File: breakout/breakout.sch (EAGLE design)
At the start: 241 parts, among them J17 1789074, J26 69168-124HLF, J29 SJ1-3514-SMT-TR, J31 69168-116HLF, J32 12226-8250-00FR, J33 1888276, J34 69168-116HLF, J35 1888276, Q1 SI1012R, Q2 SI1012R, Q3 SI1012R, Q4 SI1012R, Q5 SI1012R, Q6 SI1012R, Q7 SI1012R, Q8 SI1012R, Q9 IRFML8244TRPBF, U1 SK6805-E-J, U10 TXB0101, U11 SK6805-E-J, U12 SK6805-E-J, U13 SK6805-E-J, U14 SK6805-E-J, U15 SK6805-E-J, U16 SK6805-E-J, U17 SK6805-E-J, U18 SK6805-E-J, U19 SK6805-E-J, U2 SK6805-E-J, U20 SK6805-E-J, U21 SK6805-E-J, U22 SK6805-E-J, U23 SK6805-E-J, U24 SK6805-E-J, U25 SK6805-E-J, U26 SK6805-E-J, U27 SK6805-E-J, U28 SK6805-E-J, U29 SK6805-E-J, U3 SK6805-E-J, U30 SK6805-E-J, U31 SK6805-E-J, U32 SK6805-E-J, U33 SK6805-E-J, U34 SK6805-E-J, U35 SK6805-E-J, U36 SK6805-E-J, U37 SK6805-E-J, U38 SK6805-E-J, U39 SK6805-E-J, U4 SK6805-E-J, U40 SK6805-E-J, U41 SK6805-E-J, U42 SK6805-E-J, U43 G6K-2F-RF, U44 G6K-2F-RF, U45 G6K-2F-RF, U46 G6K-2F-RF, U47 LTM4622A, U48 SI8610, U49 TINY-FPGA-BX, U5 SK6805-E-J, U50 TCA9555, U51 FIN1032MTCX, U52 SN65LVDS9638DGN, U53 SN65LVDS9638DGN, U6 SK6805-E-J, U7 SK6805-E-J, U8 SK6805-E-J, U9 SK6805-E-J

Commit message: Updated the schematic to use Harp timestamp bus as input.
The layout (.brd) is not ready yet.

Replaced U48 SI8610 with U48 TLV70033DDCR (adds  extra BOM line. PN TLV70033DDCR)
Replaced C41 0402 0.1uF with C41 0805 10uF (same PN as C40 to not add extra BOM line)
Replaced C43 0402 0.1uF with C43 0805 10uF (same PN as C40 to not add extra BOM line)
Added R44 0402 13.3k (same PN as R19 to not add extra BOM line)
Added R45 0402 10R (adds extra BOM line. PN CRCW040210R0FKEDHP)

New BOM lines: 2
Replaced components: 3
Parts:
- added R44: 13.3k, jonnew:R_0402
- added R45: 10R, jonnew:R_0402
- C41, C43: value 0.1uF -> 10uF; device jonnew:C_0402 -> jonnew:C_0805
- U48: value SI8610 -> TLV70033DDCR; device CNP-ics 2:SI8610 -> harp input expander:TLV700XX; MPN (none) -> TLV70033DDCR; NOTES (none) -> -; TYPE (none) -> SMD
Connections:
- removed net HARP_CLKOUT: U48.A1, U49.24
- removed net N$17: C41.2, J29.5, U48.BGND
- removed net N$18: J29.4, U48.B1
- new net HARP_CLKIN: J29.4, R44.2, U49.24
- new net N$85: C43.1, R45.1, U48.OUT
- net +5V0: now also C41.1, U48.EN, U48.IN; no longer C43.2, U48.AVDD
- net GND: now also C41.2, C43.2, J29.5, U48.GND; no longer C43.1, U48.AGND
- net N$16: now also R44.1, R45.2; no longer C41.1, U48.BVDD
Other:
- note added: "HARP_CLKIN signal has the serial comunication/protocol that is synchronizing all the Harp devices."
- note removed: "CLKOUT signal has the serial comunication/protocol that will sync all the Harp devices."
- moved on the sheet: C41, C43, J29

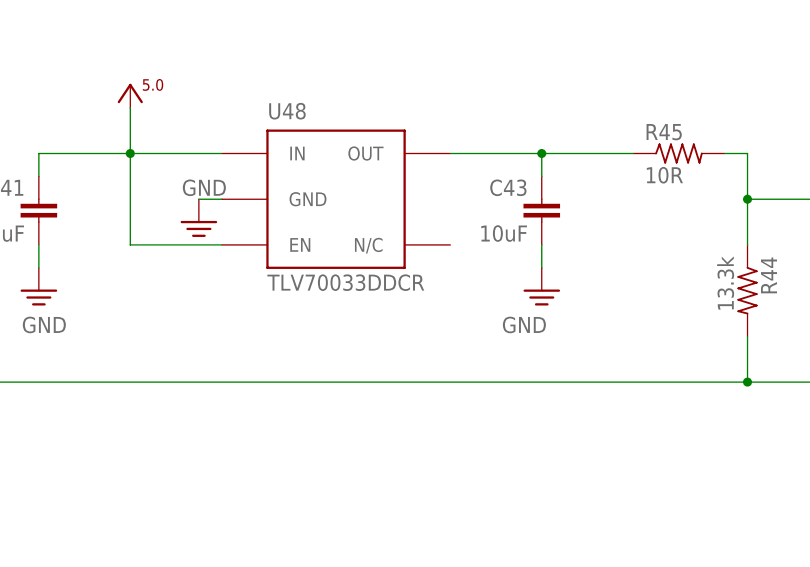
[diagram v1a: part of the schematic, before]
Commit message: Updated BOM to PN available in the market.
U48 - PN TLV70033DDCR changed to LP5951MFX-3.3/NOPB
R45 - PN CRCW040210R0FKEDHP changed to ERJ-PA2J100X
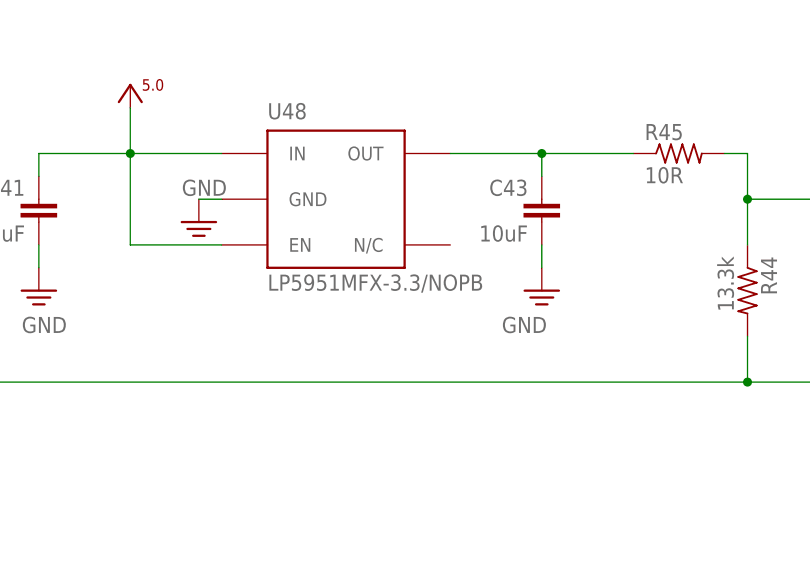
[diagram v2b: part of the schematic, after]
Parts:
- U48: value TLV70033DDCR -> LP5951MFX-3.3/NOPB
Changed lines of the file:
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@@
 <part name="R25" library="jonnew" deviceset="R" device="_0402" value="4.7k"/>
 <part name="SUPPLY9" library="jonnew" deviceset="+12V" device=""/>
-<part name="U48" library="harp input expander" deviceset="TLV700XX" device="" value="TLV70033DDCR">
+<part name="U48" library="harp input expander" deviceset="TLV700XX" device="" value="LP5951MFX-3.3/NOPB">
 <attribute name="MPN" value="TLV70033DDCR"/>
 <attribute name="NOTES" value="-"/>
